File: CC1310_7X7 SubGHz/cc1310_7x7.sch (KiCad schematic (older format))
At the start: 59 parts, among them Y2 24MHz

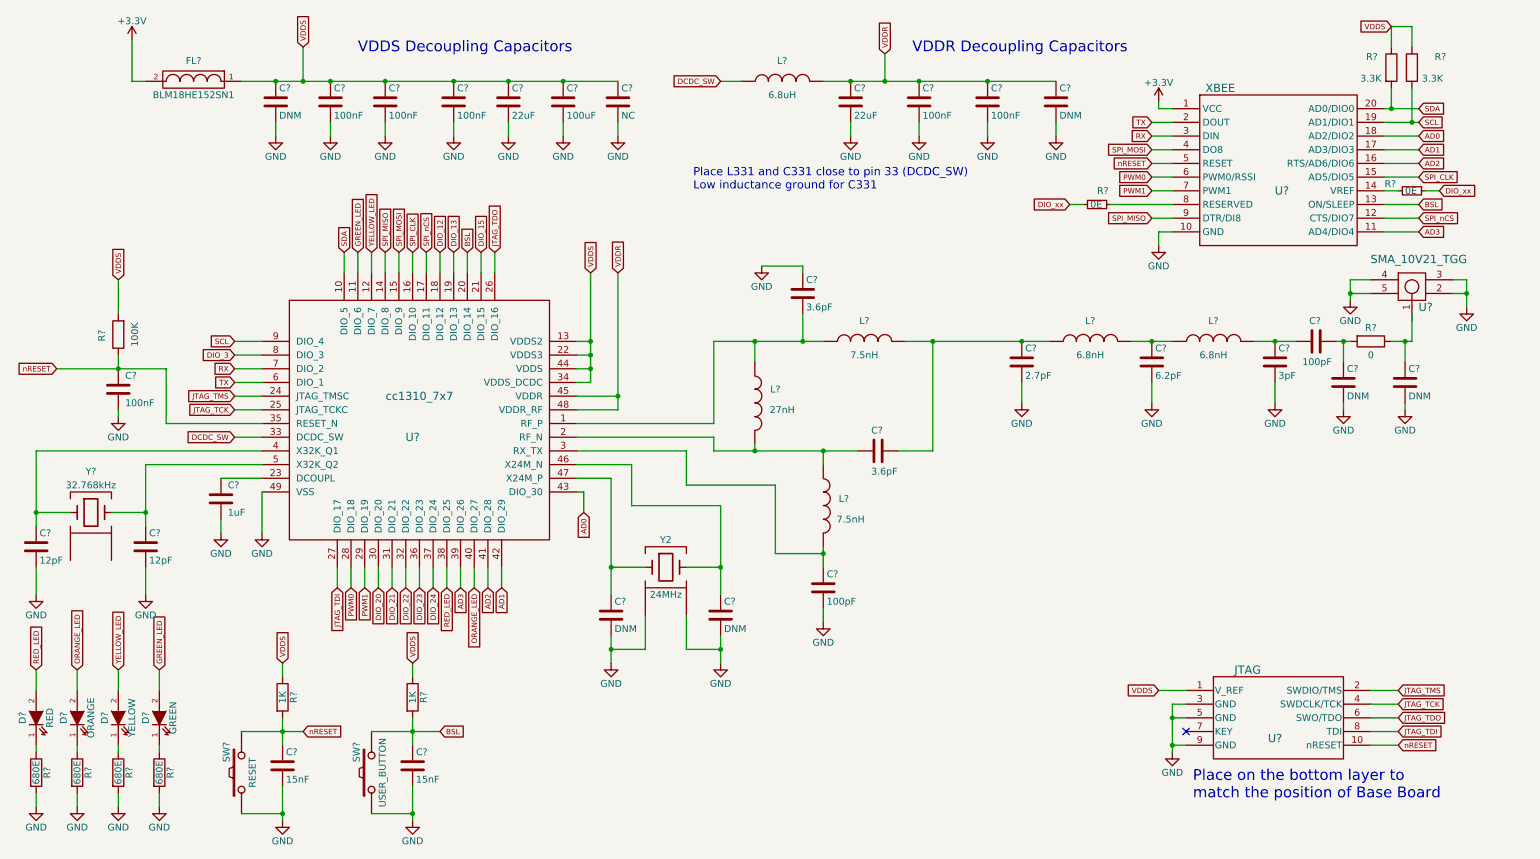
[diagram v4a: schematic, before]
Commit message: added ltr303 and Si7006 schematic
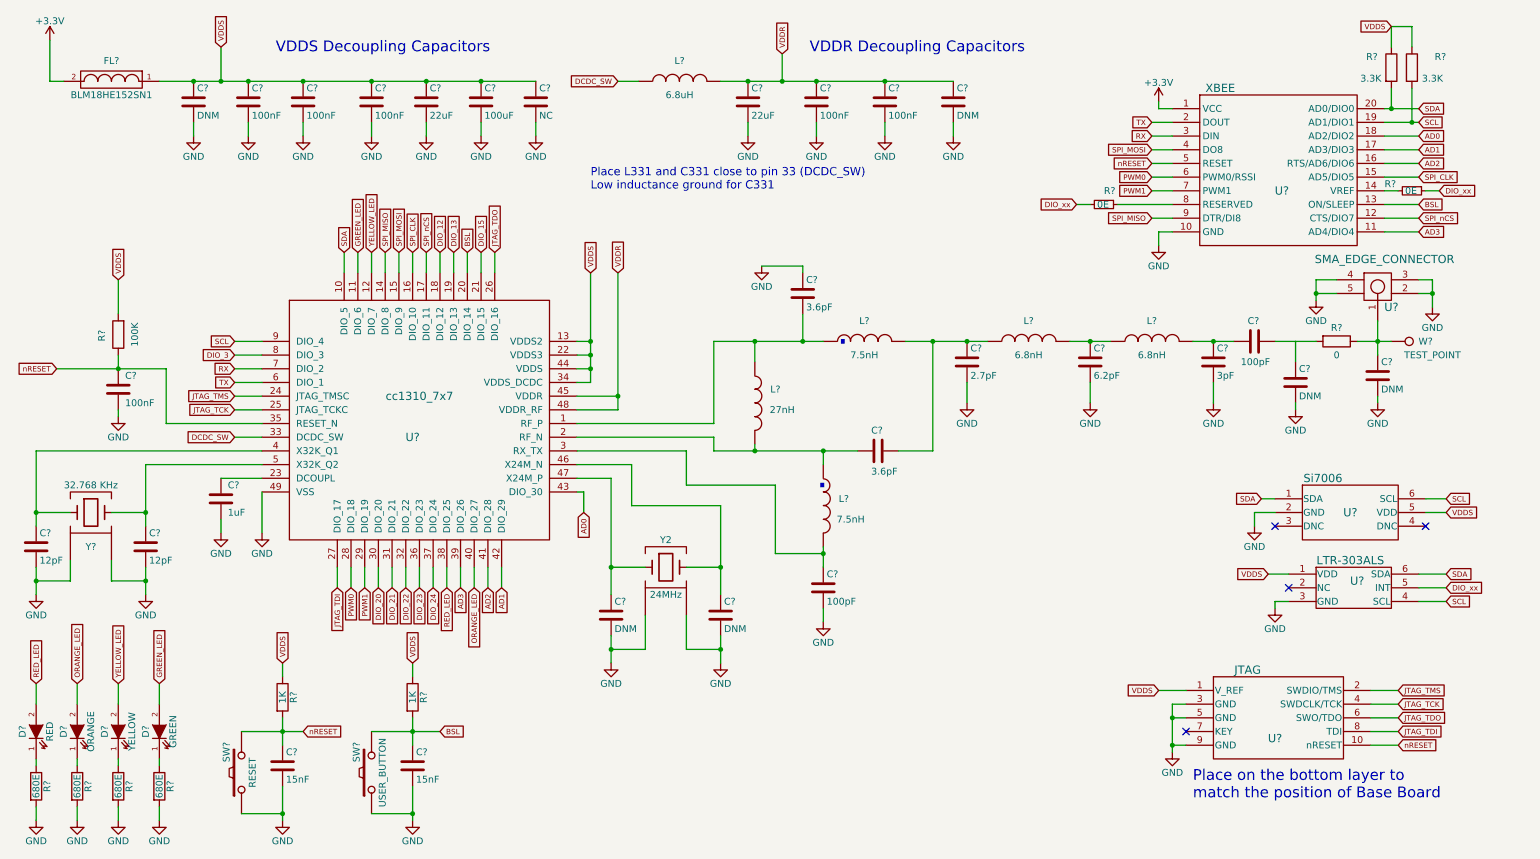
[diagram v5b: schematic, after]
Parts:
- removed U?: SMA_10V21_TGG, symbol SMA_10V21_TGG
- removed Y?: 32.768kHz, symbol Crystal
- added U?: SMA_EDGE_CONNECTOR, symbol SMA_10V21_TGG
- added U?: Si7006, symbol Si7006
- added U?: LTR-303ALS, symbol LTR-303ALS
- added W?: TEST_POINT, Wire_Pads:SolderWirePad_single_2-5mmDrill, symbol TEST_1P
- added Y?: 32.768 KHz, symbol Crystal
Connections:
- net DIO_xx: now also U?.5 (INT)
- net GND: now also U?.2, U?.2 (GND), U?.3, U?.3 (GND), U?.4, U?.5, Y?.~
- net SCL: now also U?.4 (SCL), U?.6 (SCL)
- net SDA: now also U?.1 (SDA), U?.6 (SDA)
- net VDDS: now also U?.1 (VDD), U?.5 (VDD)
- net at C?.1, U?.4 (X32K_Q1): now also Y?.1
- net at C?.1, U?.5 (X32K_Q2): now also Y?.2
- net at C?.1, R?.2: no longer C?.1
- net at C?.1, R?.1: now also U?.1, W?.1
- no-connect marks 1 -> 4
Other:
- note added: "."
- moved on the sheet: C?, D?, FL?, L?, R?

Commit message: Rev v1.0 design done
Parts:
- added P1: CONN_02X03, symbol CONN_02X03
- R12, R8: renamed from R?; value 0E -> DNM
- R9: renamed from R?; value 0 -> 0E
- gave numbers to parts that had none: 58
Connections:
- net labels added: +3V3, AD4, DIO_1, PWM2, PWM3
- net labels removed: +3.3V, DIO_12, DIO_13, DIO_3, DIO_xx
- wire segments 206 -> 212
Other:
- note added: "Place on Top layer\n2x10 2.00 mm TH male"
- note added: "Place on the bottom layer to \nmatch the position of Base Board\n2x5 1.27mm male Right Angle SMD"
- note added: "TH wire connector should also be provisioned\nalong with EDGE SMA Connector"
- note added: "To be placed on top layer"
- note added: "To be placed on top layer\ndepending on the routing\n1.27/2.0mm Male Right Angle SMD"
- note added: "change this crystal"
- note removed: "Place on the bottom layer to \nmatch the position of Base Board"
- moved on the sheet: R10, R11, R12, R8, U2, U4, U5

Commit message: arranged schematic; annotated
made specific sections in schematic
annotated the total schematic
added extra GPIO header
updated XBee and JTAG library part
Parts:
- removed U2: XBEE, symbol XBEE
- removed U3: JTAG, symbol JTAG
- added P2: XBEE, symbol XBEE
- added P3: JTAG, symbol JTAG
- renumbered U4 to U2, U5 to U3
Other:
- note added: "ADD POWER SECTION"
- note added: "Connector Section"
- note added: "POWER Section"
- note added: "Peripheral Section"
- note added: "Place L1 and C16 close to pin 33 (DCDC_SW)\nLow inductance ground for C16"
- note added: "XBee Header Section"
- note removed: "Place L331 and C331 close to pin 33 (DCDC_SW)\nLow inductance ground for C331"
- moved on the sheet: C1, C10, C14, C15, C17, C19, C2, C20, C23, C24, C25, C26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

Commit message: modified 24MHz crystal library; schematic ready without power section
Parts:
- removed Y2: 24MHz, symbol Crystal
- added Y2: crystal, symbol crystal
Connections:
- net labels added: INTR
- net labels removed: AD4, DIO_15
- wire segments 212 -> 208
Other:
- note added: "AD0: DIO_30\nAD1: DIO_29\nAD2: DIO_28\nAD3: DIO_26"
- note added: "GPIO PIN MAPPING"
- note added: "PWM0: DIO_18\nPWM1: DIO_19\nPWM2: DIO_12\nPWM3: DIO_15"
- note added: "SDA: DIO_5\nSCL: DIO_4\nINTR: DIO_13"
- note added: "SPI_MOSI: DIO_9\nSPI_MISO: DIO_8\nSPI_CLK: DIO_10\nSPI_nCS: DIO_14"
- note added: "TX: DIO_3\nRX: DIO_2"
- note removed: "ADD POWER SECTION"
- note removed: "change this crystal"
- moved on the sheet: C1, C10, C11, C12, C13, C14, C15, C16, C17, C18, C19, C2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
